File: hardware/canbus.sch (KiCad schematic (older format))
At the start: 18 parts, among them U4 MCP2515-xSO, U5 TJA1051T-3, Y1 8MHz

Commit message: Implement next hardware revision
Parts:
- R10: renamed from R15; value 1k -> 2.2k
- R9: renamed from R14; value 1k -> 2.2k
- U2: renamed from U4; symbol pi-supercap-ups-rescue:MCP2515-xSO-Custom_CAN_LIN-raspi-supercap-ups-rescue -> pi-supercap-ups:MCP2515-xSO
- U3: renamed from U5; symbol pi-supercap-ups-rescue:TJA1051T-3-Custom_CAN_LIN-raspi-supercap-ups-rescue -> pi-supercap-ups:TJA1051T-3
- renumbered C14 to C10, C12 to C11, C9 to C7, C10 to C8, C11 to C9, D13 to D10, D14 to D11, R16 to R11, R13 to R8
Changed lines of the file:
@@
 $Descr A4 11693 8268
 encoding utf-8
-Sheet 6 7
+Sheet 4 8
 Title ""
 Date ""
@@
 	4050 1650 4050 1850
 $Comp
-L power:GND #PWR034
+L power:GND #PWR028
 U 1 1 5C34A6F0
 P 2700 3050
-F 0 "#PWR034" H 2700 2800 50  0001 C CNN
+F 0 "#PWR028" H 2700 2800 50  0001 C CNN
 F 1 "GND" H 2705 2877 50  0000 C CNN
 F 2 "" H 2700 3050 50  0001 C CNN
@@
 $EndComp
 $Comp
-L power:GND #PWR038
+L power:GND #PWR033
 U 1 1 5C34A738
 P 5950 2600
-F 0 "#PWR038" H 5950 2350 50  0001 C CNN
+F 0 "#PWR033" H 5950 2350 50  0001 C CNN
 F 1 "GND" H 5955 2427 50  0000 C CNN
 F 2 "" H 5950 2600 50  0001 C CNN
@@
 $EndComp
 $Comp
-L power:GND #PWR037
+L power:GND #PWR032
 U 1 1 5C34AA94
 P 5500 1250
-F 0 "#PWR037" H 5500 1000 50  0001 C CNN
+F 0 "#PWR032" H 5500 1000 50  0001 C CNN
 F 1 "GND" H 5505 1077 50  0000 C CNN
 F 2 "" H 5500 1250 50  0001 C CNN
@@
 	2700 1000 2700 1450
 $Comp
-L Device:R R13
+L Device:R R8
 U 1 1 5C34B605
 P 3750 2650
-F 0 "R13" H 3820 2696 50  0000 L CNN
+F 0 "R8" H 3820 2696 50  0000 L CNN
 F 1 "10k" H 3820 2605 50  0000 L CNN
 F 2 "Resistor_SMD:R_0603_1608Metric_Pad1.05x0.95mm_HandSolder" V 3680 2650 50  0001 C CNN
@@
 $EndComp
 $Comp
-L Device:C C10
+L Device:C C8
 U 1 1 5C34E55A
 P 1400 3150
-F 0 "C10" H 1515 3196 50  0000 L CNN
+F 0 "C8" H 1515 3196 50  0000 L CNN
 F 1 "22pF" H 1515 3105 50  0000 L CNN
 F 2 "Capacitor_SMD:C_0603_1608Metric_Pad1.05x0.95mm_HandSolder" H 1438 3000 50  0001 C CNN
@@
 $EndComp
 $Comp
-L Device:C C9
+L Device:C C7
 U 1 1 5C34E620
 P 1100 3150
-F 0 "C9" H 985 3104 50  0000 R CNN
+F 0 "C7" H 985 3104 50  0000 R CNN
 F 1 "22pF" H 985 3195 50  0000 R CNN
 F 2 "Capacitor_SMD:C_0603_1608Metric_Pad1.05x0.95mm_HandSolder" H 1138 3000 50  0001 C CNN
@@
 $EndComp
 $Comp
-L power:GND #PWR032
+L power:GND #PWR026
 U 1 1 5C34E77C
 P 1400 3300
-F 0 "#PWR032" H 1400 3050 50  0001 C CNN
+F 0 "#PWR026" H 1400 3050 50  0001 C CNN
 F 1 "GND" H 1405 3127 50  0000 C CNN
 F 2 "" H 1400 3300 50  0001 C CNN
@@
 $EndComp
 $Comp
-L power:GND #PWR031
+L power:GND #PWR025
 U 1 1 5C34E7FF
 P 1100 3300
-F 0 "#PWR031" H 1100 3050 50  0001 C CNN
+F 0 "#PWR025" H 1100 3050 50  0001 C CNN
 F 1 "GND" H 1105 3127 50  0000 C CNN
 F 2 "" H 1100 3300 50  0001 C CNN
@@
 $EndComp
 $Comp
-L Device:R R16
+L Device:R R11
 U 1 1 5C353BFC
 P 7100 1550
-F 0 "R16" H 7170 1596 50  0000 L CNN
+F 0 "R11" H 7170 1596 50  0000 L CNN
 F 1 "120R" H 7170 1505 50  0000 L CNN
 F 2 "Resistor_SMD:R_1206_3216Metric_Pad1.42x1.75mm_HandSolder" V 7030 1550 50  0001 C CNN
@@
 	7100 1400 7100 1250
 $Comp
-L Device:C C11
+L Device:C C9
 U 1 1 5C3555AC
 P 2150 1150
-F 0 "C11" H 2265 1196 50  0000 L CNN
+F 0 "C9" H 2265 1196 50  0000 L CNN
 F 1 "47uF" H 2265 1105 50  0000 L CNN
 F 2 "Capacitor_SMD:C_0805_2012Metric_Pad1.15x1.40mm_HandSolder" H 2188 1000 50  0001 C CNN
@@
 	2150 1000 2700 1000
 $Comp
-L Device:C C12
+L Device:C C11
 U 1 1 5C356D7F
 P 5500 1100
-F 0 "C12" V 5248 1100 50  0000 C CNN
+F 0 "C11" V 5248 1100 50  0000 C CNN
 F 1 "47uF" V 5339 1100 50  0000 C CNN
 F 2 "Capacitor_SMD:C_0805_2012Metric_Pad1.15x1.40mm_HandSolder" H 5538 950 50  0001 C CNN
@@
 	5950 2450 5950 2600
 $Comp
-L pi-supercap-ups-rescue:MCP2515-xSO-Custom_CAN_LIN-raspi-supercap-ups-rescue U4
+L pi-supercap-ups:MCP2515-xSO U?
 U 1 1 5C34A611
 P 2700 2250
-F 0 "U4" H 2800 3150 50  0000 C CNN
+AR Path="/5C34A611" Ref="U?"  Part="1"
+AR Path="/5C348474/5C34A611" Ref="U2"  Part="1"
+F 0 "U2" H 2800 3150 50  0000 C CNN
 F 1 "MCP2515-xSO" H 3000 3050 50  0000 C CNN
 F 2 "Package_SO:SOIC-18W_7.5x11.6mm_P1.27mm" H 2700 1350 50  0001 C CIN
@@
 $EndComp
 $Comp
-L power:GND #PWR033
+L power:GND #PWR027
 U 1 1 5C34D248
 P 2150 1300
-F 0 "#PWR033" H 2150 1050 50  0001 C CNN
+F 0 "#PWR027" H 2150 1050 50  0001 C CNN
 F 1 "GND" H 2155 1127 50  0000 C CNN
 F 2 "" H 2150 1300 50  0001 C CNN
@@
 5V
 $Comp
-L pi-supercap-ups-rescue:TJA1051T-3-Custom_CAN_LIN-raspi-supercap-ups-rescue U5
+L pi-supercap-ups:TJA1051T-3 U3
 U 1 1 5C5F35CC
 P 5950 1950
-F 0 "U5" H 6050 2450 50  0000 C CNN
+F 0 "U3" H 6050 2450 50  0000 C CNN
 F 1 "TJA1051T-3" H 6200 2350 50  0000 C CNN
 F 2 "Package_SO:SOIC-8_3.9x4.9mm_P1.27mm" H 5950 1450 50  0001 C CIN
@@
 	3300 1750 4200 1750
 $Comp
-L Device:LED D13
+L Device:LED D10
 U 1 1 5C63AE4E
 P 4200 2750
-F 0 "D13" V 4238 2633 50  0000 R CNN
+F 0 "D10" V 4238 2633 50  0000 R CNN
 F 1 "GLED" V 4147 2633 50  0000 R CNN
 F 2 "LED_SMD:LED_0603_1608Metric_Pad1.05x0.95mm_HandSolder" H 4200 2750 50  0001 C CNN
@@
 $EndComp
 $Comp
-L Device:LED D14
+L Device:LED D11
 U 1 1 5C63AF79
 P 4600 2750
-F 0 "D14" V 4638 2633 50  0000 R CNN
+F 0 "D11" V 4638 2633 50  0000 R CNN
 F 1 "GLED" V 4547 2633 50  0000 R CNN
 F 2 "LED_SMD:LED_0603_1608Metric_Pad1.05x0.95mm_HandSolder" H 4600 2750 50  0001 C CNN
@@
 $EndComp
 $Comp
-L Device:R R14
+L Device:R R9
 U 1 1 5C63B109
 P 4200 2250
-F 0 "R14" H 4270 2296 50  0000 L CNN
-F 1 "1k" H 4270 2205 50  0000 L CNN
+F 0 "R9" H 4270 2296 50  0000 L CNN
+F 1 "2.2k" H 4270 2205 50  0000 L CNN
 F 2 "Resistor_SMD:R_0603_1608Metric_Pad1.05x0.95mm_HandSolder" V 4130 2250 50  0001 C CNN
 F 3 "~" H 4200 2250 50  0001 C CNN
@@
 $EndComp
 $Comp
-L Device:R R15
+L Device:R R10
 U 1 1 5C63B229
 P 4600 2250
-F 0 "R15" H 4670 2296 50  0000 L CNN
-F 1 "1k" H 4670 2205 50  0000 L CNN
+F 0 "R10" H 4670 2296 50  0000 L CNN
+F 1 "2.2k" H 4670 2205 50  0000 L CNN
 F 2 "Resistor_SMD:R_0603_1608Metric_Pad1.05x0.95mm_HandSolder" V 4530 2250 50  0001 C CNN
 F 3 "~" H 4600 2250 50  0001 C CNN
@@
 $EndComp
 $Comp
-L power:GND #PWR035
+L power:GND #PWR029
 U 1 1 5C63B348
 P 4200 3000
-F 0 "#PWR035" H 4200 2750 50  0001 C CNN
+F 0 "#PWR029" H 4200 2750 50  0001 C CNN
 F 1 "GND" H 4205 2827 50  0000 C CNN
 F 2 "" H 4200 3000 50  0001 C CNN
@@
 $EndComp
 $Comp
-L power:GND #PWR036
+L power:GND #PWR030
 U 1 1 5C63B441
 P 4600 3000
-F 0 "#PWR036" H 4600 2750 50  0001 C CNN
+F 0 "#PWR030" H 4600 2750 50  0001 C CNN
 F 1 "GND" H 4605 2827 50  0000 C CNN
 F 2 "" H 4600 3000 50  0001 C CNN
@@
 Connection ~ 4600 1850
 $Comp
-L Device:C C14
+L Device:C C10
 U 1 1 5C66D5F2
 P 5100 2350
-F 0 "C14" V 4848 2350 50  0000 C CNN
+F 0 "C10" V 4848 2350 50  0000 C CNN
 F 1 "100nF" V 4939 2350 50  0000 C CNN
 F 2 "Capacitor_SMD:C_0603_1608Metric_Pad1.05x0.95mm_HandSolder" H 5138 2200 50  0001 C CNN
@@
 	5100 2050 5450 2050
 $Comp
-L power:GND #PWR0101
+L power:GND #PWR031
 U 1 1 5C66ED33
 P 5100 2600
-F 0 "#PWR0101" H 5100 2350 50  0001 C CNN
+F 0 "#PWR031" H 5100 2350 50  0001 C CNN
 F 1 "GND" H 5105 2427 50  0000 C CNN
 F 2 "" H 5100 2600 50  0001 C CNN

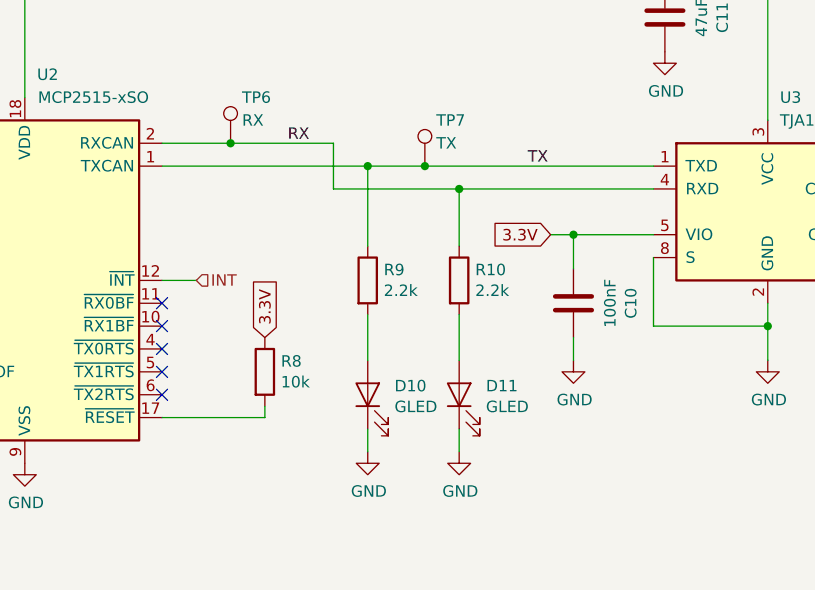
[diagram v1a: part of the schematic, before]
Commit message: Changed to pure-serial topology. Changed to beefier mcu.
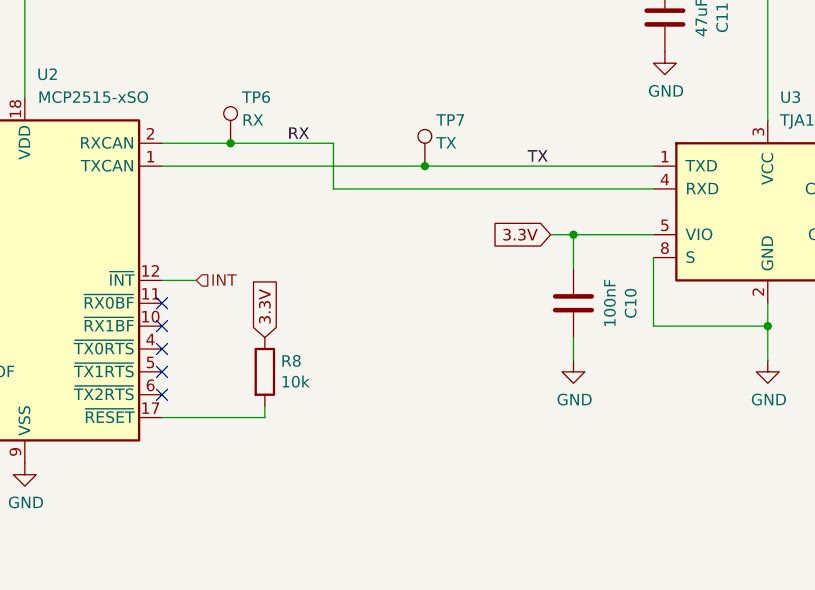
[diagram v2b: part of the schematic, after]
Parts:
- removed D10, D11: GLED, LED_SMD:LED_0603_1608Metric_Pad1.05x0.95mm_HandSolder, symbol Device:LED
- removed R10, R9: 2.2k, Resistor_SMD:R_0603_1608Metric_Pad1.05x0.95mm_HandSolder, symbol Device:R
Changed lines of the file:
@@
-EESchema Schematic File Version 4
+EESchema Schematic File Version 5
 LIBS:pi-supercap-ups-cache
-EELAYER 26 0
+EELAYER 30 0
 EELAYER END
 $Descr A4 11693 8268
 encoding utf-8
-Sheet 4 8
+Sheet 3 8
 Title ""
 Date ""
@@
 Connection ~ 6700 2050
 Wire Wire Line
-	6700 2050 7250 2050
-Wire Wire Line
 	7100 1400 7100 1250
 $Comp
@@
 Wire Wire Line
 	5500 950  5950 950
-Wire Wire Line
-	4050 1850 4600 1850
-Wire Wire Line
-	3300 1750 4200 1750
-$Comp
-L Device:LED D10
-U 1 1 5C63AE4E
-P 4200 2750
-F 0 "D10" V 4238 2633 50  0000 R CNN
-F 1 "GLED" V 4147 2633 50  0000 R CNN
-F 2 "LED_SMD:LED_0603_1608Metric_Pad1.05x0.95mm_HandSolder" H 4200 2750 50  0001 C CNN
-F 3 "~" H 4200 2750 50  0001 C CNN
-	1    4200 2750
-	0    -1   -1   0
-$EndComp
-$Comp
-L Device:LED D11
-U 1 1 5C63AF79
-P 4600 2750
-F 0 "D11" V 4638 2633 50  0000 R CNN
-F 1 "GLED" V 4547 2633 50  0000 R CNN
-F 2 "LED_SMD:LED_0603_1608Metric_Pad1.05x0.95mm_HandSolder" H 4600 2750 50  0001 C CNN
-F 3 "~" H 4600 2750 50  0001 C CNN
-	1    4600 2750
-	0    -1   -1   0
-$EndComp
-$Comp
-L Device:R R9
-U 1 1 5C63B109
-P 4200 2250
-F 0 "R9" H 4270 2296 50  0000 L CNN
-F 1 "2.2k" H 4270 2205 50  0000 L CNN
-F 2 "Resistor_SMD:R_0603_1608Metric_Pad1.05x0.95mm_HandSolder" V 4130 2250 50  0001 C CNN
-F 3 "~" H 4200 2250 50  0001 C CNN
-	1    4200 2250
-	1    0    0    -1
-$EndComp
-$Comp
-L Device:R R10
-U 1 1 5C63B229
-P 4600 2250
-F 0 "R10" H 4670 2296 50  0000 L CNN
-F 1 "2.2k" H 4670 2205 50  0000 L CNN
-F 2 "Resistor_SMD:R_0603_1608Metric_Pad1.05x0.95mm_HandSolder" V 4530 2250 50  0001 C CNN
-F 3 "~" H 4600 2250 50  0001 C CNN
-	1    4600 2250
-	1    0    0    -1
-$EndComp
-$Comp
-L power:GND #PWR029
-U 1 1 5C63B348
-P 4200 3000
-F 0 "#PWR029" H 4200 2750 50  0001 C CNN
-F 1 "GND" H 4205 2827 50  0000 C CNN
-F 2 "" H 4200 3000 50  0001 C CNN
-F 3 "" H 4200 3000 50  0001 C CNN
-	1    4200 3000
-	1    0    0    -1
-$EndComp
-$Comp
-L power:GND #PWR030
-U 1 1 5C63B441
-P 4600 3000
-F 0 "#PWR030" H 4600 2750 50  0001 C CNN
-F 1 "GND" H 4605 2827 50  0000 C CNN
-F 2 "" H 4600 3000 50  0001 C CNN
-F 3 "" H 4600 3000 50  0001 C CNN
-	1    4600 3000
-	1    0    0    -1
-$EndComp
-Wire Wire Line
-	4200 3000 4200 2900
-Wire Wire Line
-	4600 2900 4600 3000
-Wire Wire Line
-	4600 2600 4600 2400
-Wire Wire Line
-	4200 2400 4200 2600
-Wire Wire Line
-	4200 2100 4200 1750
-Connection ~ 4200 1750
-Wire Wire Line
-	4200 1750 4450 1750
-Wire Wire Line
-	4600 2100 4600 1850
 $Comp
 L Connector:TestPoint TP6
@@
 	4450 1750 5450 1750
 Connection ~ 4450 1750
-Wire Wire Line
-	4600 1850 5450 1850
-Connection ~ 4600 1850
 $Comp
 L Device:C C10
@@
 Text Label 1950 2550 3    50   ~ 0
 OSC1
+Wire Wire Line
+	3300 1750 4450 1750
+Wire Wire Line
+	4050 1850 5450 1850
+Wire Wire Line
+	6700 2050 7250 2050
 $EndSCHEMATC

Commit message: revE ready for production
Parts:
- removed C7, C8: 22pF, Capacitor_SMD:C_0603_1608Metric_Pad1.05x0.95mm_HandSolder, symbol Device:C
- removed R8: 10k, Resistor_SMD:R_0603_1608Metric_Pad1.05x0.95mm_HandSolder, symbol Device:R
- removed TP6: RX, TestPoint:TestPoint_Keystone_5000-5004_Miniature, symbol Connector:TestPoint
- removed TP7: TX, TestPoint:TestPoint_Keystone_5000-5004_Miniature, symbol Connector:TestPoint
- removed U2: MCP2515-xSO, Package_SO:SOIC-18W_7.5x11.6mm_P1.27mm, symbol pi-supercap-ups:MCP2515-xSO
- removed U3: TJA1051T-3, Package_SO:SOIC-8_3.9x4.9mm_P1.27mm, symbol pi-supercap-ups:TJA1051T-3
- removed Y1: 8MHz, Crystal:Crystal_HC49-U_Vertical, symbol Device:Crystal
- added C3, C4, C5: 100nF, Capacitor_SMD:C_0603_1608Metric_Pad1.05x0.95mm_HandSolder, symbol Device:C
- added IC1, IC2: MCP25625T-E_ML, custom:QFN65P600X600X100-29M-D, symbol pi-supercap-ups:MCP25625T-E_ML
- added JP2: Term, Connector_PinHeader_2.54mm:PinHeader_1x02_P2.54mm_Vertical, symbol Jumper:Jumper_2_Open
- added R21, R24, R25, R29, R30: 10k, Resistor_SMD:R_0603_1608Metric_Pad1.05x0.95mm_HandSolder, symbol Device:R
- added R31: 120R, Resistor_SMD:R_1206_3216Metric_Pad1.42x1.75mm_HandSolder, symbol Device:R
- added X1: S3D8.000000B20F30T, Oscillator:Oscillator_SMD_Abracon_ASE-4Pin_3.2x2.5mm, symbol Oscillator:ASE-xxxMHz
- C11, C9: value 47uF -> 100nF; footprint Capacitor_SMD:C_0805_2012Metric_Pad1.15x1.40mm_HandSolder -> Capacitor_SMD:C_0603_1608Metric_Pad1.05x0.95mm_HandSolder
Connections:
- net 3.3V: now also C10.1, C3.1, C4.1, IC1.11 (VIO), IC1.3 (VDD), IC2.11 (VIO), IC2.3 (VDD), R21.1, R24.2, R25.1, R29.1, R30.1, X1.4 (Vdd); no longer C10.2
- net 5V: now also C11.1, C5.1, IC1.19 (VDDA), IC2.19 (VDDA); no longer C11.2
- net GND: now also C10.2, C11.2, C3.2, C4.2, C5.2, IC1.15 (STBY), IC1.18 (VSS), IC1.22 (GND), IC1.29 (EXP), IC2.15 (STBY), IC2.18 (VSS), IC2.22 (GND), IC2.29 (EXP), X1.2 (GND); no longer C10.1, C11.1
- net SCK: now also IC1.26 (SCK), IC2.26 (SCK)
- net SI: now also IC1.27 (SI), IC2.27 (SI)
- net SO: now also IC1.28 (SO), IC2.28 (SO)
- net CAN_H renamed CAN0_H
- net CAN0_H: now also IC1.13 (CANH)
- net CAN_L renamed CAN0_L
- net CAN0_L: now also IC1.12 (CANL)
- net OSC1 renamed OSC_OUT
- net OSC_OUT: now also IC1.21 (OSC1), IC2.21 (OSC1), X1.3 (OUT)
- new net: IC1.10 (RXD), IC1.5 (RXCAN)
- new net: IC1.16 (TXD), IC1.4 (TXCAN)
- new net: IC2.10 (RXD), IC2.5 (RXCAN)
- new net: IC2.16 (TXD), IC2.4 (TXCAN)
- new net: JP2.2 (B), R31.1
- new net CAN1_H: IC2.13 (CANH), R31.2
- new net CAN1_L: IC2.12 (CANL), JP2.1 (A)
- new net CS0: IC1.1 (~CS), R21.2
- new net CS1: IC2.1 (~CS), R29.2
- new net INT0: IC1.25 (~INT), R25.2
- new net INT1: IC2.25 (~INT), R30.2
- new net ~RESET: IC1.2 (~RESET), IC2.2 (~RESET), R24.1
- no-connect marks 6 -> 19
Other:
- note added: "CAN bus 0 controller + tranceiver"
- note added: "CAN bus 1 controller + tranceiver"
- note added: "Oscillator shared by both CAN controllers"
- moved on the sheet: JP1, R11, TP5
